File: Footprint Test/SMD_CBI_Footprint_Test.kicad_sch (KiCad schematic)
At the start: 9 parts, among them J1 Conn_01x04

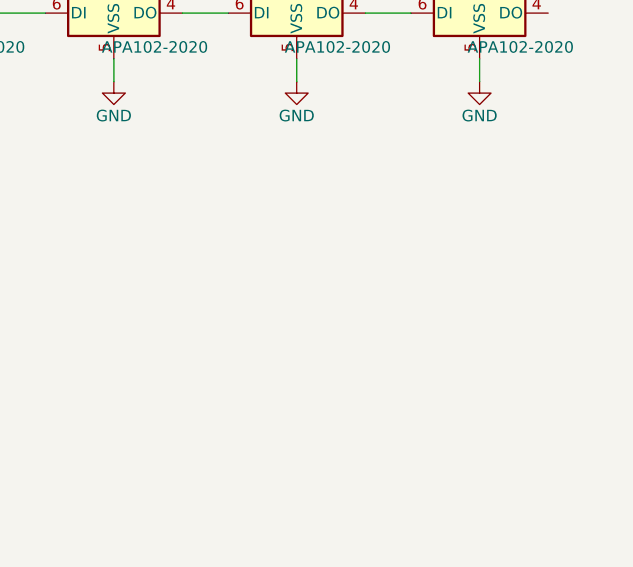
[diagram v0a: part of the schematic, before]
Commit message: Add courtyard to footprints. Create external KiCad library.
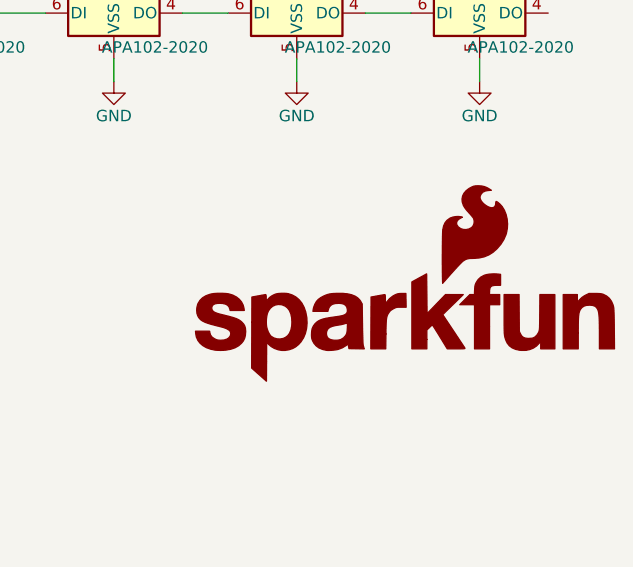
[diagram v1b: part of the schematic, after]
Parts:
- added G1: SparkFun_Logo, symbol SparkFun-Aesthetic:SparkFun_Logo
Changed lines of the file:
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@@
+	)
+	(symbol
+		(lib_id "SparkFun-Aesthetic:SparkFun_Logo")
+		(at 172.72 96.52 0)
+		(unit 1)
+		(exclude_from_sim no)
+		(in_bom yes)
+		(on_board no)
+		(dnp no)
+		(fields_autoplaced yes)
+		(property "Reference" "G1"
+			(at 172.72 90.17 0)
+			(effects
+				(font
+					(size 1.27 1.27)
+				)
+				(hide yes)
+			)
+		)
+		(property "Value" "SparkFun_Logo"
+			(at 172.72 101.6 0)
+			(effects
+				(font
+					(size 1.27 1.27)
+				)
+				(hide yes)
+			)
+		)
+		(property "Footprint" ""
+			(at 172.72 104.14 0)
+			(effects
+				(font
+					(size 1.27 1.27)
+				)
+				(hide yes)
+			)
+		)
+		(property "Datasheet" ""
+			(at 176.533 92.7212 0)
+			(effects
+				(font
+					(size 1.27 1.27)
+				)
+				(hide yes)
+			)
+		)
+		(property "Description" ""
+			(at 172.72 96.52 0)
+			(effects
+				(font
+					(size 1.27 1.27)
+				)
+				(hide yes)
+			)
+		)
+		(instances
+			(project ""
+				(path "/5d0a92af-9337-4b37-be64-ada206601254"
+					(reference "G1")
+					(unit 1)
+				)
+			)
+		)
 	)
 	(symbol
